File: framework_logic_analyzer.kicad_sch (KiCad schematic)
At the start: 61 parts, among them IC5 CYUSB3014-BZXC, J3 Conn_ARM_JTAG_SWD_10, Q1 MMBT3904, Q2 MMBT3904, Q3 MMBT3904, U5 M24M02-DR, Y1 19.200 MHz

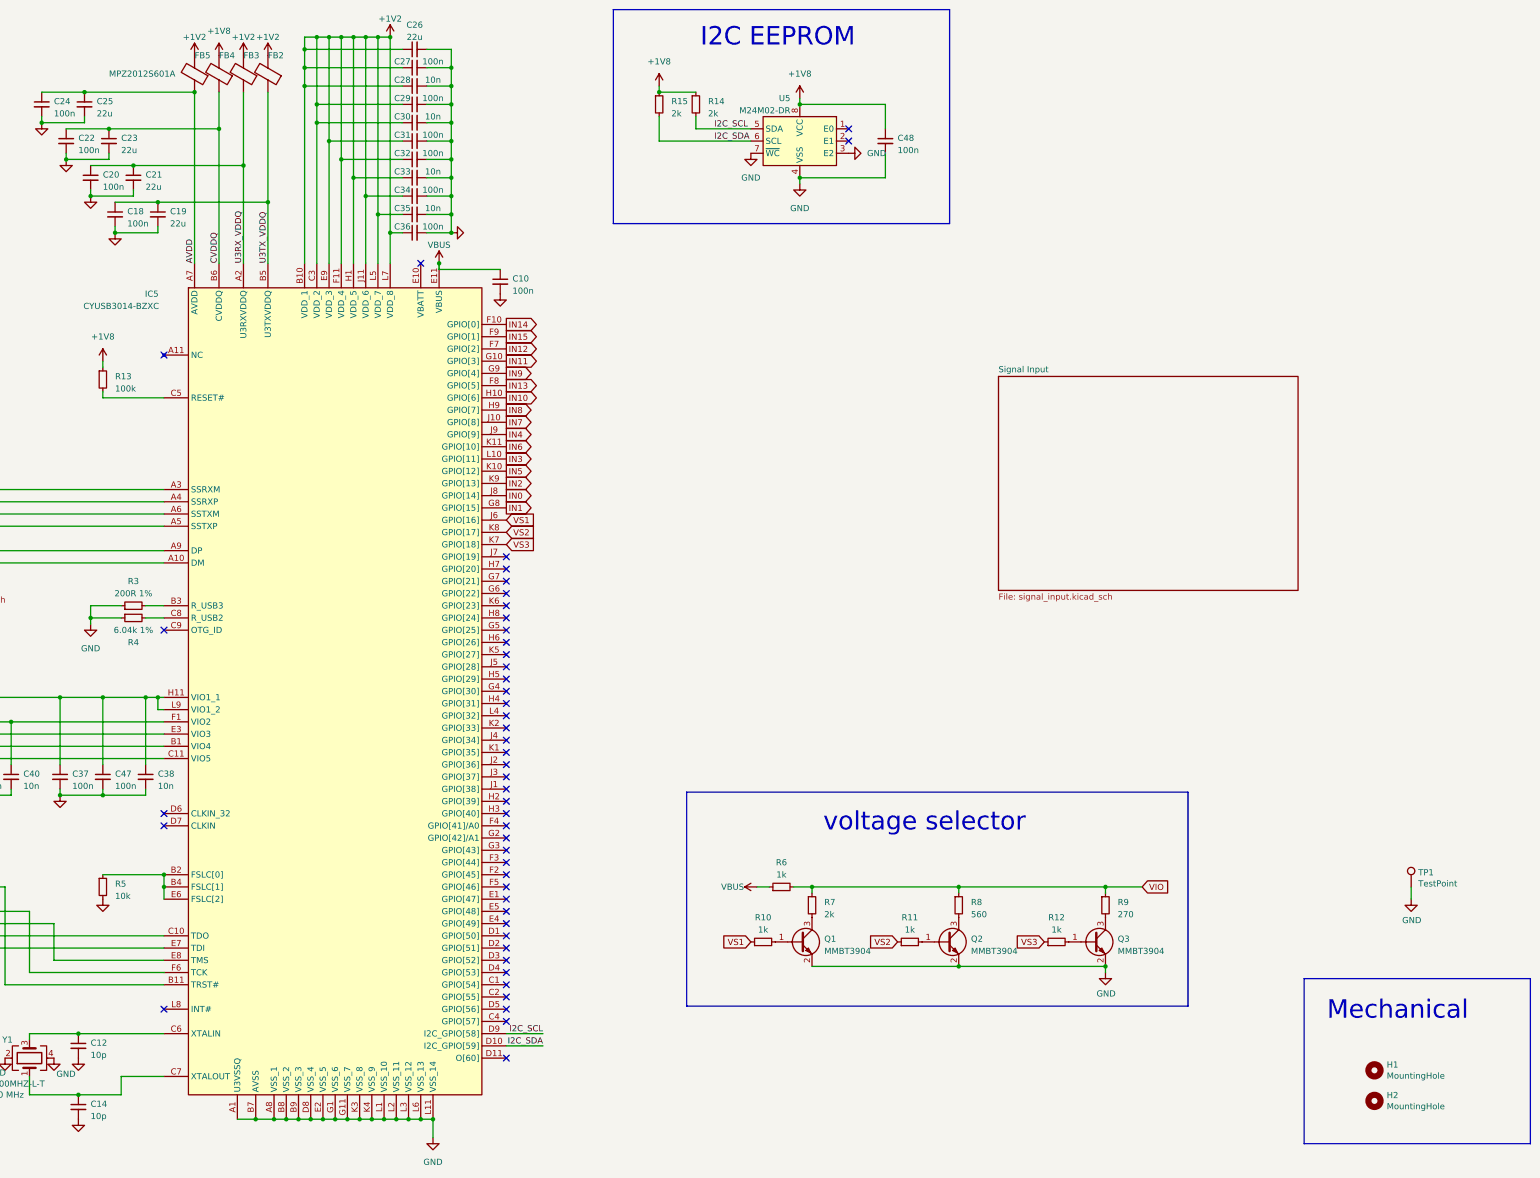
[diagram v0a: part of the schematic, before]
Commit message: start implementing SML feedback
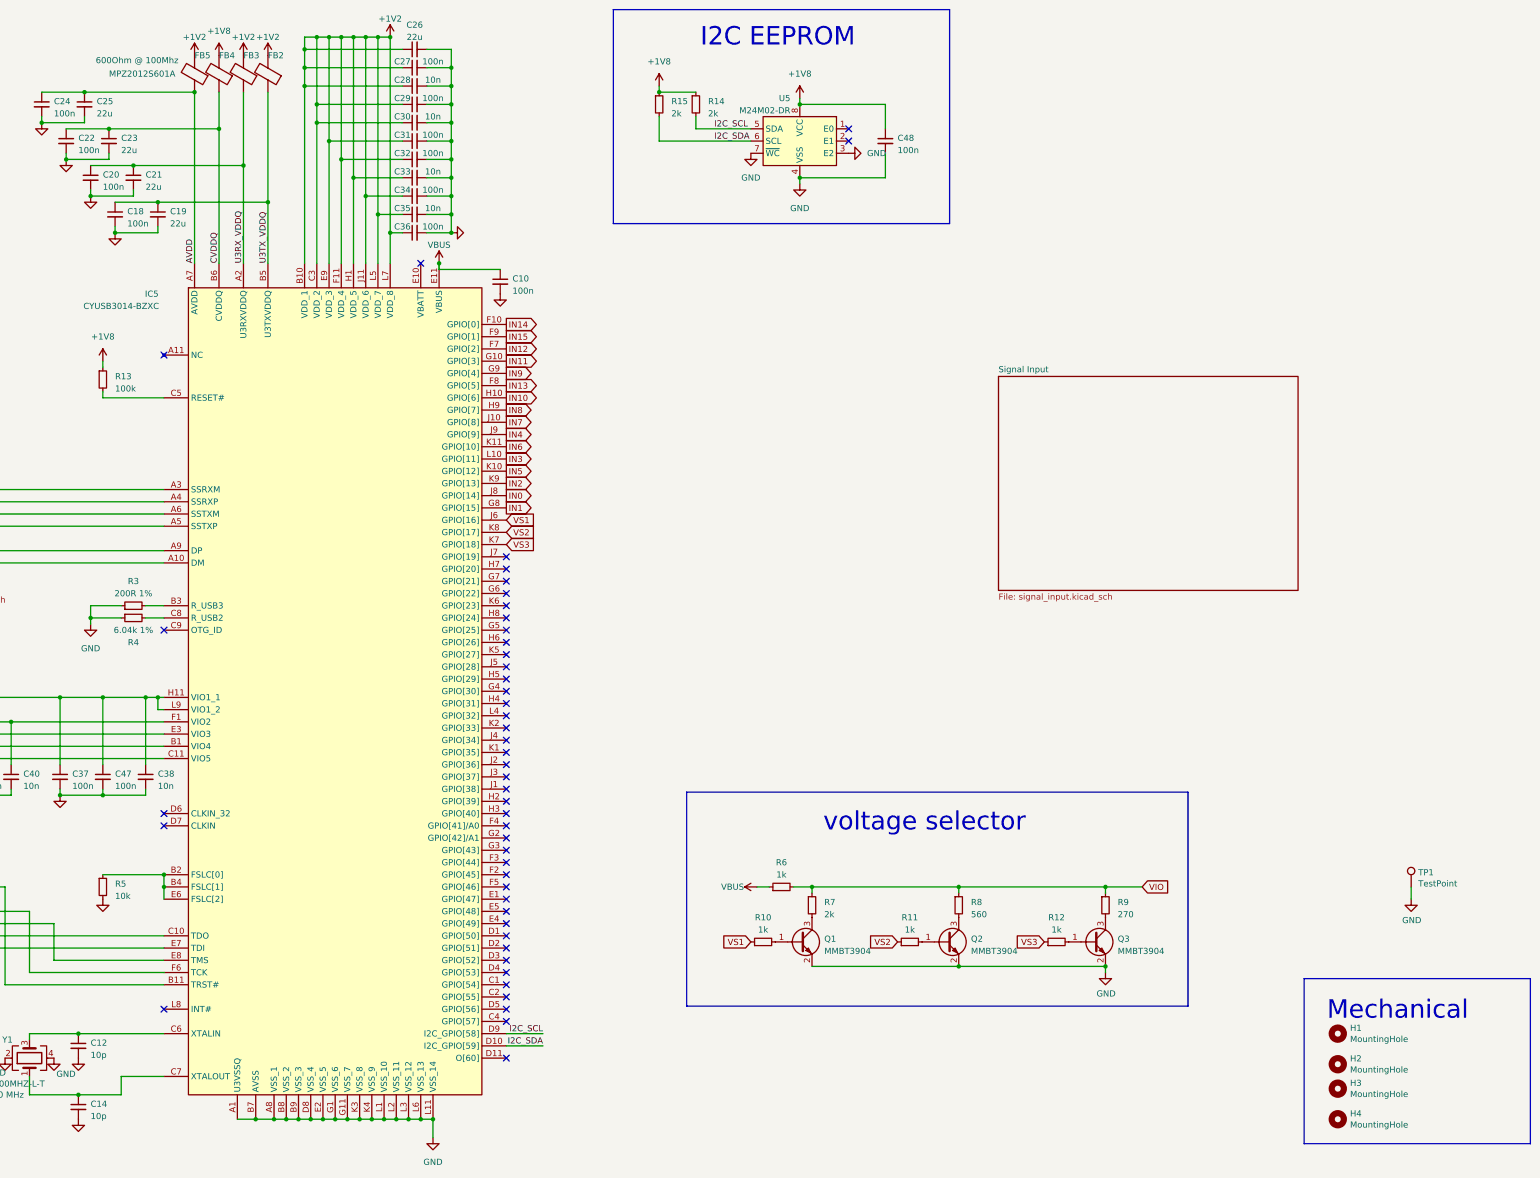
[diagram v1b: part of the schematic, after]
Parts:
- added H3, H4: MountingHole, MountingHole:MountingHole_2.2mm_M2, symbol Mechanical:MountingHole
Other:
- moved on the sheet: H1, H2
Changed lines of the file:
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@@
 	)
 	(symbol
+		(lib_id "Mechanical:MountingHole")
+		(at 364.49 237.49 0)
+		(unit 1)
+		(exclude_from_sim no)
+		(in_bom yes)
+		(on_board yes)
+		(dnp no)
+		(property "Reference" "H3"
+			(at 367.03 236.3216 0)
+			(effects
+				(font
+					(size 1.27 1.27)
+				)
+				(justify left)
+			)
+		)
+		(property "Value" "MountingHole"
+			(at 367.03 238.633 0)
+			(effects
+				(font
+					(size 1.27 1.27)
+				)
+				(justify left)
+			)
+		)
+		(property "Footprint" "MountingHole:MountingHole_2.2mm_M2"
+			(at 364.49 237.49 0)
+			(effects
+				(font
+					(size 1.27 1.27)
+				)
+				(hide yes)
+			)
+		)
+		(property "Datasheet" "~"
+			(at 364.49 237.49 0)
+			(effects
+				(font
+					(size 1.27 1.27)
+				)
+				(hide yes)
+			)
+		)
+		(property "Description" ""
+			(at 364.49 237.49 0)
+			(effects
+				(font
+					(size 1.27 1.27)
+				)
+			)
+		)
+		(instances
+			(project "framework_logic_analyzer"
+				(path "/cec59c69-8f0d-4d06-8fee-6cd1bb72d09c"
+					(reference "H3")
+					(unit 1)
+				)
+			)
+		)
+	)
+	(symbol
 		(lib_id "Device:FerriteBead")
 		(at 142.24 26.67 180)
@@
 			)
 		)
-		(property "Description" ""
-			(at 127 26.67 0)
+		(property "Description" "600Ohm @ 100Mhz"
+			(at 115.062 23.876 0)
 			(effects
 				(font
@@
 	)
 	(symbol
+		(lib_id "Mechanical:MountingHole")
+		(at 364.49 243.84 0)
+		(unit 1)
+		(exclude_from_sim no)
+		(in_bom yes)
+		(on_board yes)
+		(dnp no)
+		(property "Reference" "H4"
+			(at 367.03 242.6716 0)
+			(effects
+				(font
+					(size 1.27 1.27)
+				)
+				(justify left)
+			)
+		)
+		(property "Value" "MountingHole"
+			(at 367.03 244.983 0)
+			(effects
+				(font
+					(size 1.27 1.27)
+				)
+				(justify left)
+			)
+		)
+		(property "Footprint" "MountingHole:MountingHole_2.2mm_M2"
+			(at 364.49 243.84 0)
+			(effects
+				(font
+					(size 1.27 1.27)
+				)
+				(hide yes)
+			)
+		)
+		(property "Datasheet" "~"
+			(at 364.49 243.84 0)
+			(effects
+				(font
+					(size 1.27 1.27)
+				)
+				(hide yes)
+			)
+		)
+		(property "Description" ""
+			(at 364.49 243.84 0)
+			(effects
+				(font
+					(size 1.27 1.27)
+				)
+			)
+		)
+		(instances
+			(project "framework_logic_analyzer"
+				(path "/cec59c69-8f0d-4d06-8fee-6cd1bb72d09c"
+					(reference "H4")
+					(unit 1)
+				)
+			)
+		)
+	)
+	(symbol
 		(lib_id "Device:R_Small")
 		(at 245.11 207.01 90)
@@
 	(symbol
 		(lib_id "Mechanical:MountingHole")
-		(at 372.11 233.68 0)
+		(at 364.49 226.06 0)
 		(unit 1)
 		(exclude_from_sim no)
@@
 		(dnp no)
 		(property "Reference" "H1"
-			(at 374.65 232.5116 0)
+			(at 367.03 224.8916 0)
 			(effects
 				(font
@@
 		)
 		(property "Value" "MountingHole"
-			(at 374.65 234.823 0)
+			(at 367.03 227.203 0)
 			(effects
 				(font
@@
 		)
 		(property "Footprint" "MountingHole:MountingHole_2.2mm_M2"
-			(at 372.11 233.68 0)
+			(at 364.49 226.06 0)
 			(effects
 				(font
@@
 		)
 		(property "Datasheet" "~"
-			(at 372.11 233.68 0)
+			(at 364.49 226.06 0)
 			(effects
 				(font
@@
 		)
 		(property "Description" ""
-			(at 372.11 233.68 0)
+			(at 364.49 226.06 0)
 			(effects
 				(font
@@
 	(symbol
 		(lib_id "Mechanical:MountingHole")
-		(at 372.11 240.03 0)
+		(at 364.49 232.41 0)
 		(unit 1)
 		(exclude_from_sim no)
@@
 		(dnp no)
 		(property "Reference" "H2"
-			(at 374.65 238.8616 0)
+			(at 367.03 231.2416 0)
 			(effects
 				(font
@@
 		)
 		(property "Value" "MountingHole"
-			(at 374.65 241.173 0)
+			(at 367.03 233.553 0)
 			(effects
 				(font
@@
 		)
 		(property "Footprint" "MountingHole:MountingHole_2.2mm_M2"
-			(at 372.11 240.03 0)
+			(at 364.49 232.41 0)
 			(effects
 				(font
@@
 		)
 		(property "Datasheet" "~"
-			(at 372.11 240.03 0)
+			(at 364.49 232.41 0)
 			(effects
 				(font
@@
 		)
 		(property "Description" ""
-			(at 372.11 240.03 0)
+			(at 364.49 232.41 0)
 			(effects
 				(font
